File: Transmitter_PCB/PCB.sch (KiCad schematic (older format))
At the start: 47 parts, among them J1 Conn_01x04_Female, J10 Conn_01x08_Female, J11 Conn_01x01_Female, J12 Conn_01x04_Female, J13 Conn_01x02_Female, J2 Conn_01x28_Female, J3 Conn_01x02_Female, J4 Conn_01x02_Female, J5 Conn_01x02_Female, J6 Conn_01x02_Female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

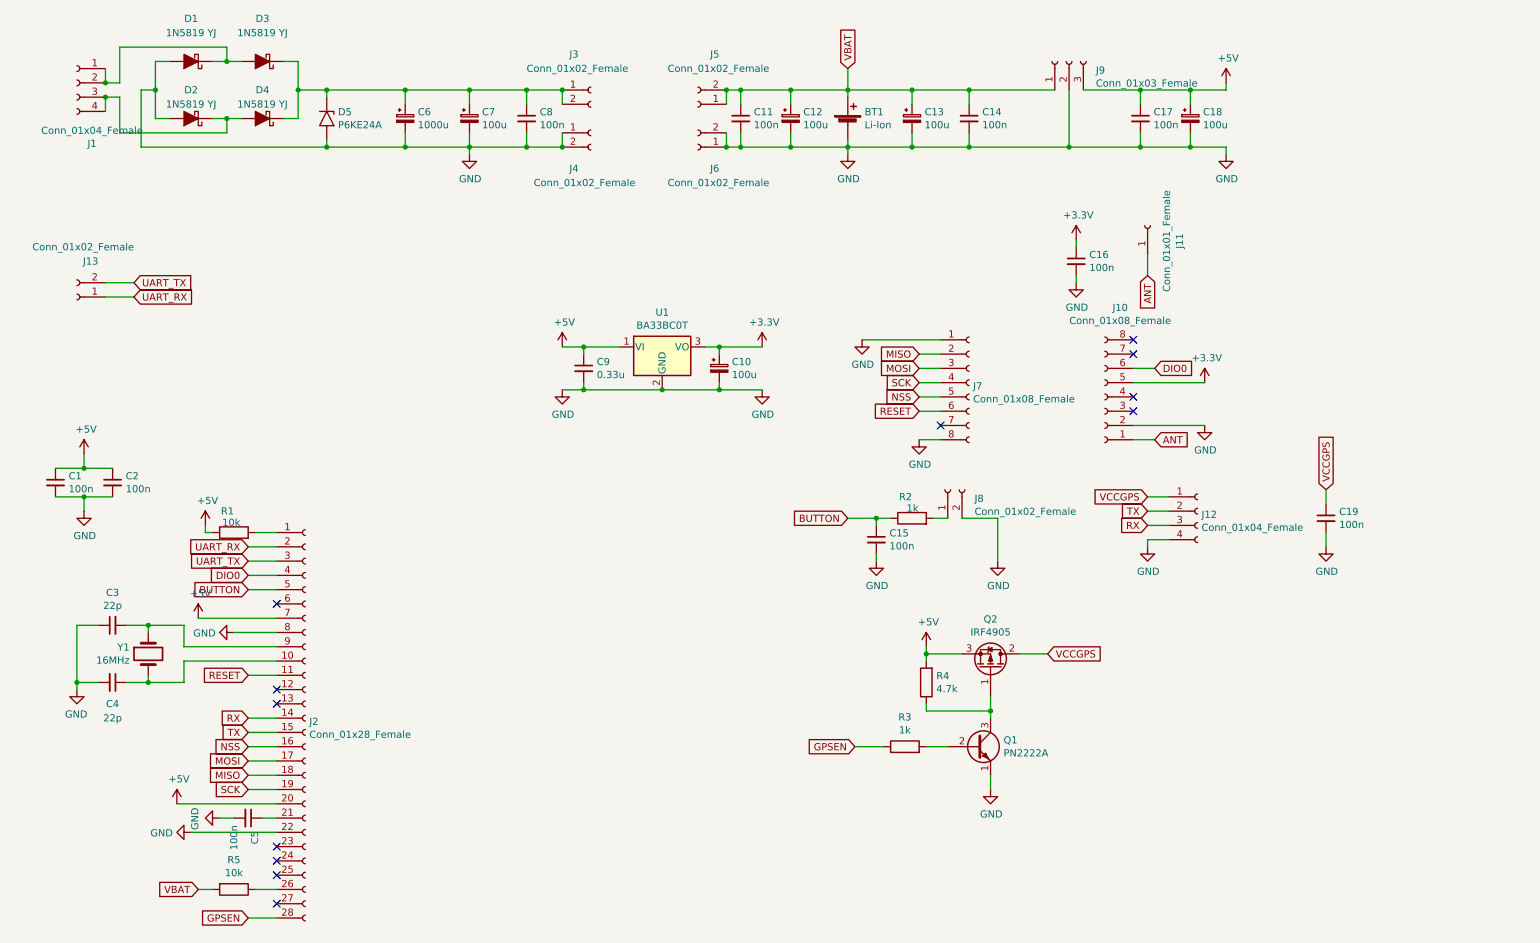
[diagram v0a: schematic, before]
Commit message: Fixed LoRa socket
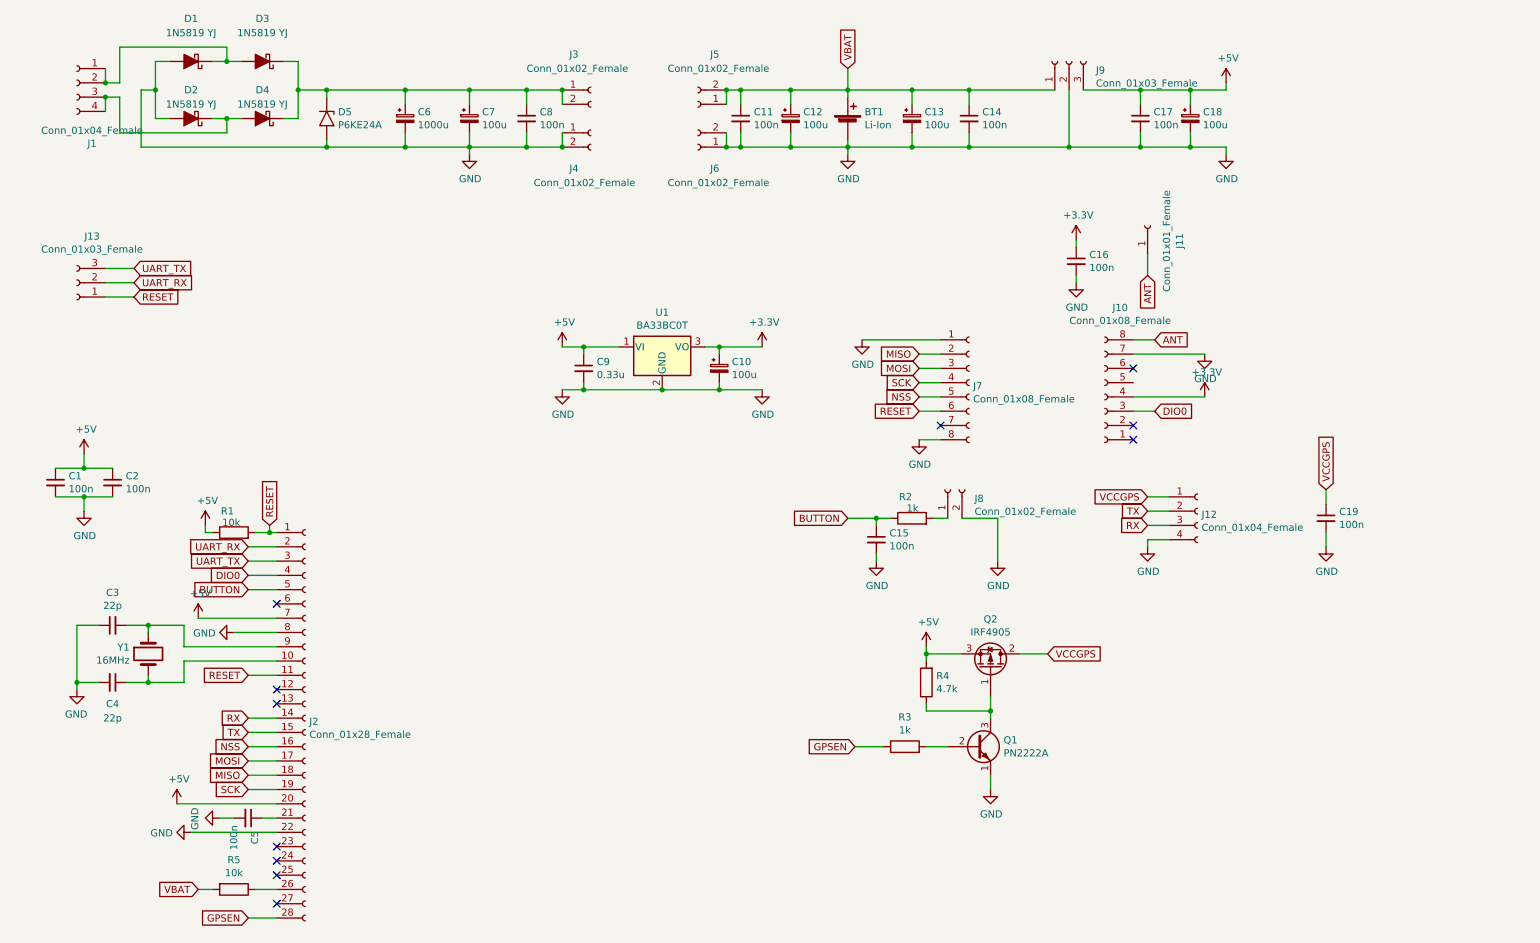
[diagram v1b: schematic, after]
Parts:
- removed J13: Conn_01x02_Female, Connector_PinSocket_2.54mm:PinSocket_1x02_P2.54mm_Vertical, symbol Connector:Conn_01x02_Female
- added J13: Conn_01x03_Female, Connector_PinSocket_2.54mm:PinSocket_1x03_P2.54mm_Vertical, symbol Connector:Conn_01x03_Female
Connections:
- net +3V3: now also J10.4 (Pin_4); no longer J10.5 (Pin_5)
- net ANT: now also J10.8 (Pin_8); no longer J10.1 (Pin_1)
- net DIO0: now also J10.3 (Pin_3); no longer J10.6 (Pin_6)
- net GND: now also J10.7 (Pin_7); no longer J10.2 (Pin_2)
- net RESET: now also J2.1 (Pin_1), R1.2, J13.1 (Pin_1)
- net UART_RX: now also J13.2 (Pin_2)
- net UART_TX: now also J13.3 (Pin_3)
- no-connect marks 12 -> 11
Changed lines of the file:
@@
 	1    0    0    -1
 $EndComp
-NoConn ~ 8850 3000
-NoConn ~ 8850 3500
-NoConn ~ 8850 3400
-Wire Wire Line
-	9000 3200 8850 3200
-Wire Wire Line
-	9000 3700 8850 3700
-Text GLabel 9000 3200 2    50   Input ~ 0
-DIO0
-Wire Wire Line
-	8850 3300 9350 3300
+Wire Wire Line
+	9000 3000 8850 3000
+Wire Wire Line
+	8850 3400 9350 3400
 $Comp
 L power:+3.3V #PWR022
 U 1 1 5E58D10D
-P 9350 3300
-F 0 "#PWR022" H 9350 3150 50  0001 C CNN
-F 1 "+3.3V" H 9365 3473 50  0000 C CNN
-F 2 "" H 9350 3300 50  0001 C CNN
-F 3 "" H 9350 3300 50  0001 C CNN
-	1    9350 3300
-	1    0    0    -1
-$EndComp
-Wire Wire Line
-	8850 3600 9350 3600
-$Comp
-L power:GND #PWR023
-U 1 1 5E5A485A
-P 9350 3600
-F 0 "#PWR023" H 9350 3350 50  0001 C CNN
-F 1 "GND" H 9355 3427 50  0000 C CNN
-F 2 "" H 9350 3600 50  0001 C CNN
-F 3 "" H 9350 3600 50  0001 C CNN
-	1    9350 3600
+P 9350 3400
+F 0 "#PWR022" H 9350 3250 50  0001 C CNN
+F 1 "+3.3V" H 9365 3573 50  0000 C CNN
+F 2 "" H 9350 3400 50  0001 C CNN
+F 3 "" H 9350 3400 50  0001 C CNN
+	1    9350 3400
 	1    0    0    -1
 $EndComp
@@
 	0    -1   -1   0
 $EndComp
-Text GLabel 9000 3700 2    50   Input ~ 0
+Text GLabel 9000 3000 2    50   Input ~ 0
 ANT
 Wire Wire Line
@@
 ANT
 Wire Wire Line
-	2700 4350 2850 4350
+	2700 4350 2800 4350
 $Comp
 L Device:R R1
@@
 Connection ~ 1650 1200
 Connection ~ 1650 1300
-NoConn ~ 8850 3100
-$Comp
-L Connector:Conn_01x02_Female J13
-U 1 1 5E38F499
-P 1450 2700
-F 0 "J13" H 1300 2450 50  0000 L CNN
-F 1 "Conn_01x02_Female" H 1050 2350 50  0000 L CNN
-F 2 "Connector_PinSocket_2.54mm:PinSocket_1x02_P2.54mm_Vertical" H 1450 2700 50  0001 C CNN
-F 3 "~" H 1450 2700 50  0001 C CNN
-	1    1450 2700
-	-1   0    0    1
-$EndComp
 Text GLabel 2650 4450 0    50   Input ~ 0
 UART_RX
@@
 Wire Wire Line
 	2850 4550 2650 4550
-Text GLabel 1850 2700 2    50   Input ~ 0
+Text GLabel 1850 2600 2    50   Input ~ 0
 UART_RX
-Wire Wire Line
-	1650 2700 1850 2700
-Text GLabel 1850 2600 2    50   Input ~ 0
+Text GLabel 1850 2500 2    50   Input ~ 0
 UART_TX
-Wire Wire Line
-	1650 2600 1850 2600
 $Comp
 L Device:R R5
@@
 Text GLabel 2300 6850 0    50   Input ~ 0
 VBAT
+NoConn ~ 8850 3700
+NoConn ~ 8850 3600
+Wire Wire Line
+	9000 3500 8850 3500
+Text GLabel 9000 3500 2    50   Input ~ 0
+DIO0
+NoConn ~ 8850 3200
+Wire Wire Line
+	8850 3100 9350 3100
+$Comp
+L power:GND #PWR0101
+U 1 1 5E431489
+P 9350 3100
+F 0 "#PWR0101" H 9350 2850 50  0001 C CNN
+F 1 "GND" H 9355 2927 50  0000 C CNN
+F 2 "" H 9350 3100 50  0001 C CNN
+F 3 "" H 9350 3100 50  0001 C CNN
+	1    9350 3100
+	1    0    0    -1
+$EndComp
+$Comp
+L Connector:Conn_01x03_Female J13
+U 1 1 5E44D686
+P 1450 2600
+F 0 "J13" H 1344 2275 50  0000 C CNN
+F 1 "Conn_01x03_Female" H 1344 2366 50  0000 C CNN
+F 2 "Connector_PinSocket_2.54mm:PinSocket_1x03_P2.54mm_Vertical" H 1450 2600 50  0001 C CNN
+F 3 "~" H 1450 2600 50  0001 C CNN
+	1    1450 2600
+	-1   0    0    1
+$EndComp
+Text GLabel 2800 4300 1    50   Input ~ 0
+RESET
+Wire Wire Line
+	2800 4350 2800 4300
+Connection ~ 2800 4350
+Wire Wire Line
+	2800 4350 2850 4350
+Wire Wire Line
+	1650 2700 1850 2700
+Text GLabel 1850 2700 2    50   Input ~ 0
+RESET
+Wire Wire Line
+	1650 2500 1850 2500
+Wire Wire Line
+	1650 2600 1850 2600
 $EndSCHEMATC

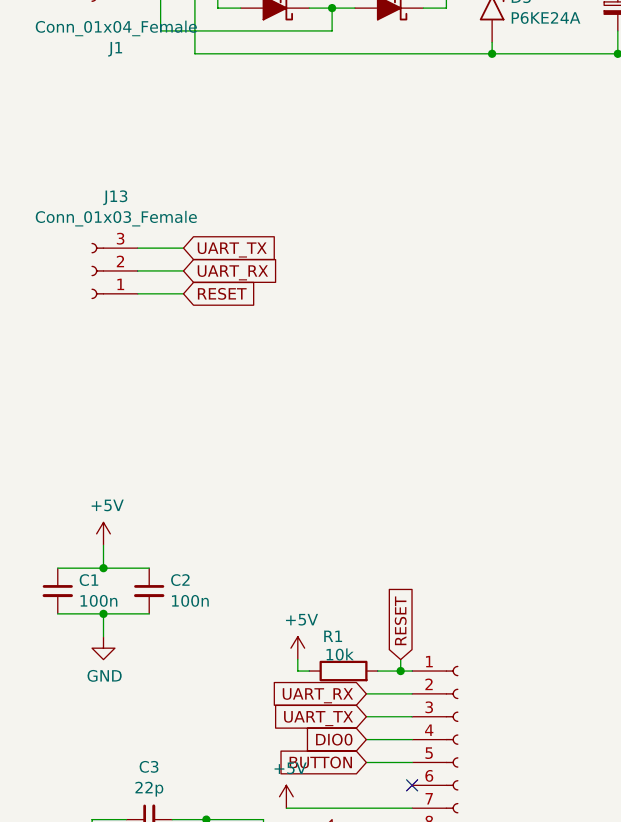
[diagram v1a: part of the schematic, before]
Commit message: Fixed Transmitter PCB Spacing
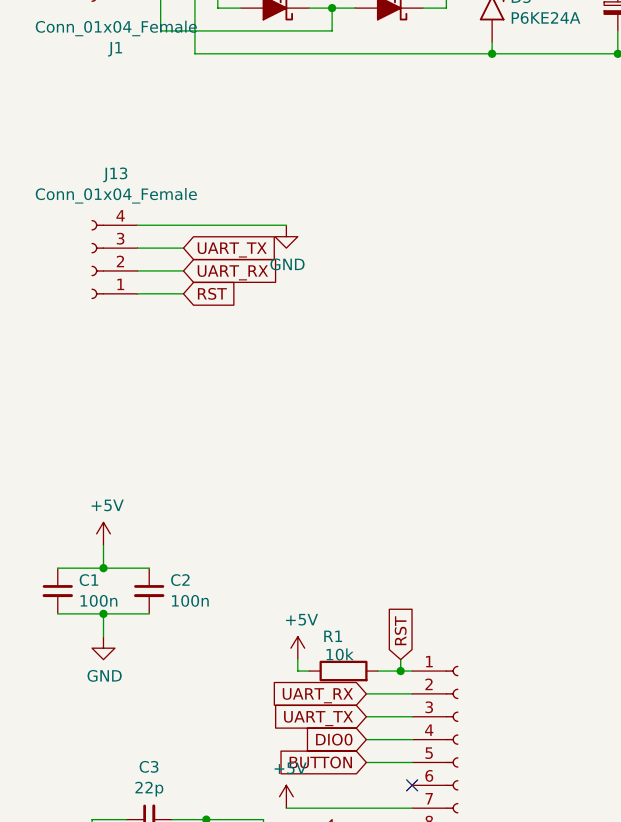
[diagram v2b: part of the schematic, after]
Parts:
- removed J13: Conn_01x03_Female, Connector_PinSocket_2.54mm:PinSocket_1x03_P2.54mm_Vertical, symbol Connector:Conn_01x03_Female
- added J13: Conn_01x04_Female, Connector_PinSocket_2.54mm:PinSocket_1x04_P2.54mm_Vertical, symbol Connector:Conn_01x04_Female
- J8: footprint Connector_Molex:Molex_PicoBlade_53047-0210_1x02_P1.25mm_Vertical -> Connector_Molex:Molex_KK-254_AE-6410-02A_1x02_P2.54mm_Vertical
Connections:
- net GND: now also J13.4 (Pin_4)
- net RESET: no longer J2.1 (Pin_1), R1.2
- net UART_RX: now also J13.2 (Pin_2)
- net UART_TX: now also J13.3 (Pin_3)
- new net RST: J13.1 (Pin_1), J2.1 (Pin_1), R1.2
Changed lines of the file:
@@
 F 0 "J8" V 7488 3862 50  0000 R CNN
 F 1 "Conn_01x02_Female" V 7397 3862 50  0000 R CNN
-F 2 "Connector_Molex:Molex_PicoBlade_53047-0210_1x02_P1.25mm_Vertical" H 7550 4050 50  0001 C CNN
+F 2 "Connector_Molex:Molex_KK-254_AE-6410-02A_1x02_P2.54mm_Vertical" H 7550 4050 50  0001 C CNN
 F 3 "~" H 7550 4050 50  0001 C CNN
 	1    7550 4050
@@
 Connection ~ 6000 1250
 Connection ~ 6000 1650
-Wire Wire Line
-	7700 1650 8400 1650
 Connection ~ 8400 1650
 Wire Wire Line
@@
 	8400 1250 8400 1650
 Wire Wire Line
-	7700 1250 8300 1250
-Wire Wire Line
 	8500 1250 8900 1250
 NoConn ~ 2850 6650
@@
 	1    0    0    -1
 $EndComp
-$Comp
-L Connector:Conn_01x03_Female J13
-U 1 1 5E44D686
+Text GLabel 2800 4300 1    50   Input ~ 0
+RST
+Wire Wire Line
+	2800 4350 2800 4300
+Connection ~ 2800 4350
+Wire Wire Line
+	2800 4350 2850 4350
+Wire Wire Line
+	1650 2700 1850 2700
+Text GLabel 1850 2700 2    50   Input ~ 0
+RST
+Wire Wire Line
+	1650 2500 1850 2500
+Wire Wire Line
+	1650 2600 1850 2600
+Wire Wire Line
+	7700 1650 8400 1650
+Wire Wire Line
+	7700 1250 8300 1250
+$Comp
+L Connector:Conn_01x04_Female J13
+U 1 1 5E4E3087
 P 1450 2600
-F 0 "J13" H 1344 2275 50  0000 C CNN
-F 1 "Conn_01x03_Female" H 1344 2366 50  0000 C CNN
-F 2 "Connector_PinSocket_2.54mm:PinSocket_1x03_P2.54mm_Vertical" H 1450 2600 50  0001 C CNN
+F 0 "J13" H 1344 2175 50  0000 C CNN
+F 1 "Conn_01x04_Female" H 1344 2266 50  0000 C CNN
+F 2 "Connector_PinSocket_2.54mm:PinSocket_1x04_P2.54mm_Vertical" H 1450 2600 50  0001 C CNN
 F 3 "~" H 1450 2600 50  0001 C CNN
 	1    1450 2600
 	-1   0    0    1
 $EndComp
-Text GLabel 2800 4300 1    50   Input ~ 0
-RESET
-Wire Wire Line
-	2800 4350 2800 4300
-Connection ~ 2800 4350
-Wire Wire Line
-	2800 4350 2850 4350
-Wire Wire Line
-	1650 2700 1850 2700
-Text GLabel 1850 2700 2    50   Input ~ 0
-RESET
-Wire Wire Line
-	1650 2500 1850 2500
-Wire Wire Line
-	1650 2600 1850 2600
+Wire Wire Line
+	1650 2400 2300 2400
+$Comp
+L power:GND #PWR0102
+U 1 1 5E4FFF60
+P 2300 2400
+F 0 "#PWR0102" H 2300 2150 50  0001 C CNN
+F 1 "GND" H 2305 2227 50  0000 C CNN
+F 2 "" H 2300 2400 50  0001 C CNN
+F 3 "" H 2300 2400 50  0001 C CNN
+	1    2300 2400
+	1    0    0    -1
+$EndComp
 $EndSCHEMATC

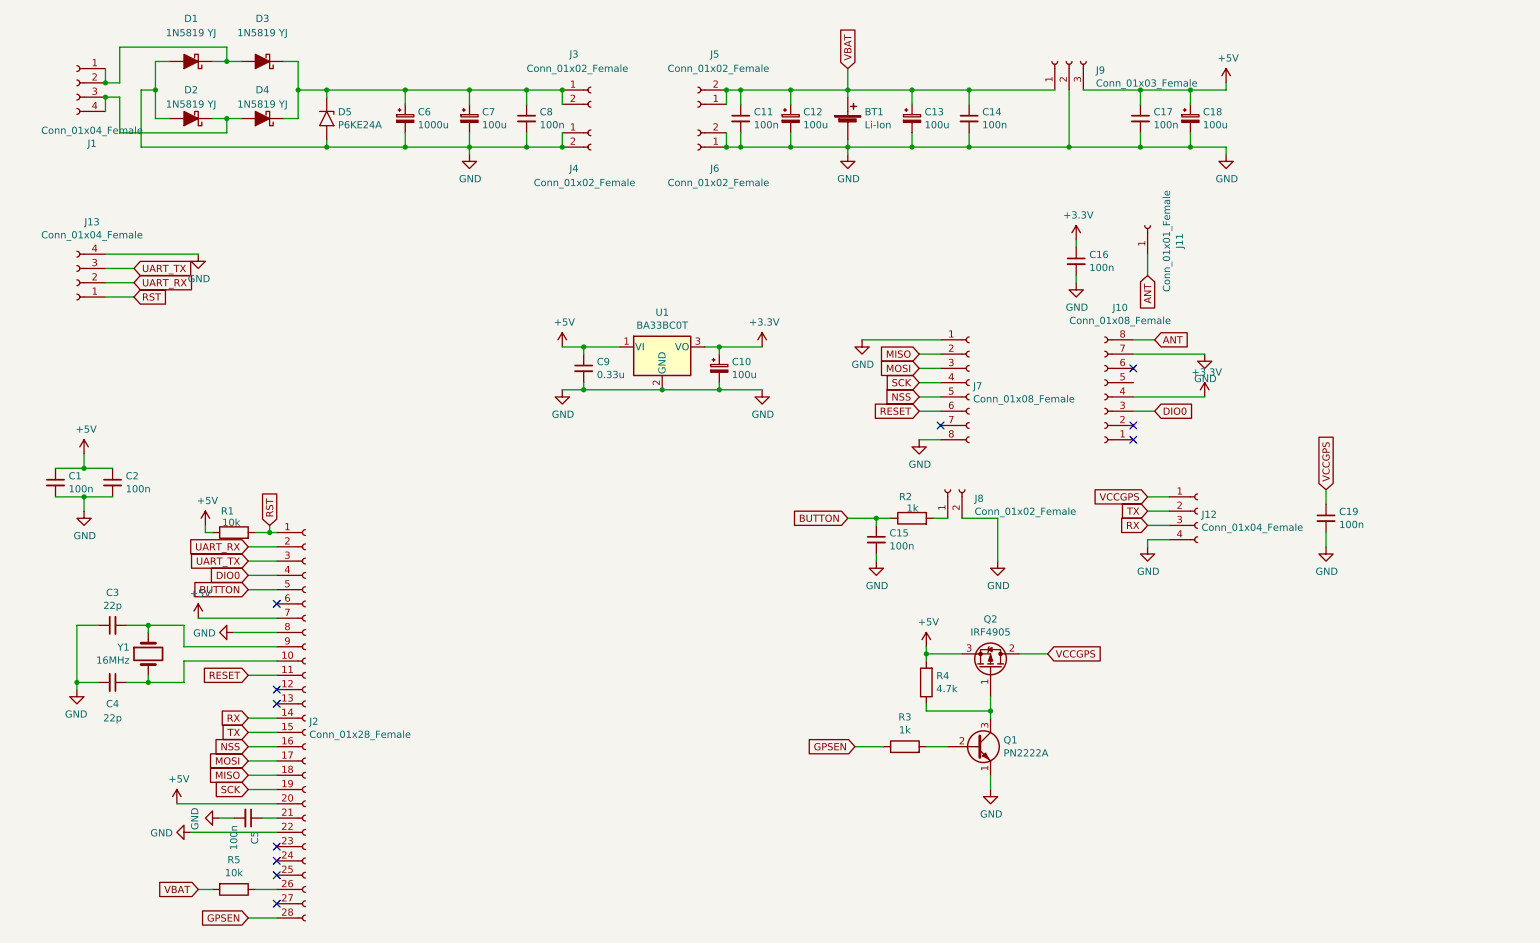
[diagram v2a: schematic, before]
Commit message: Added 3d models
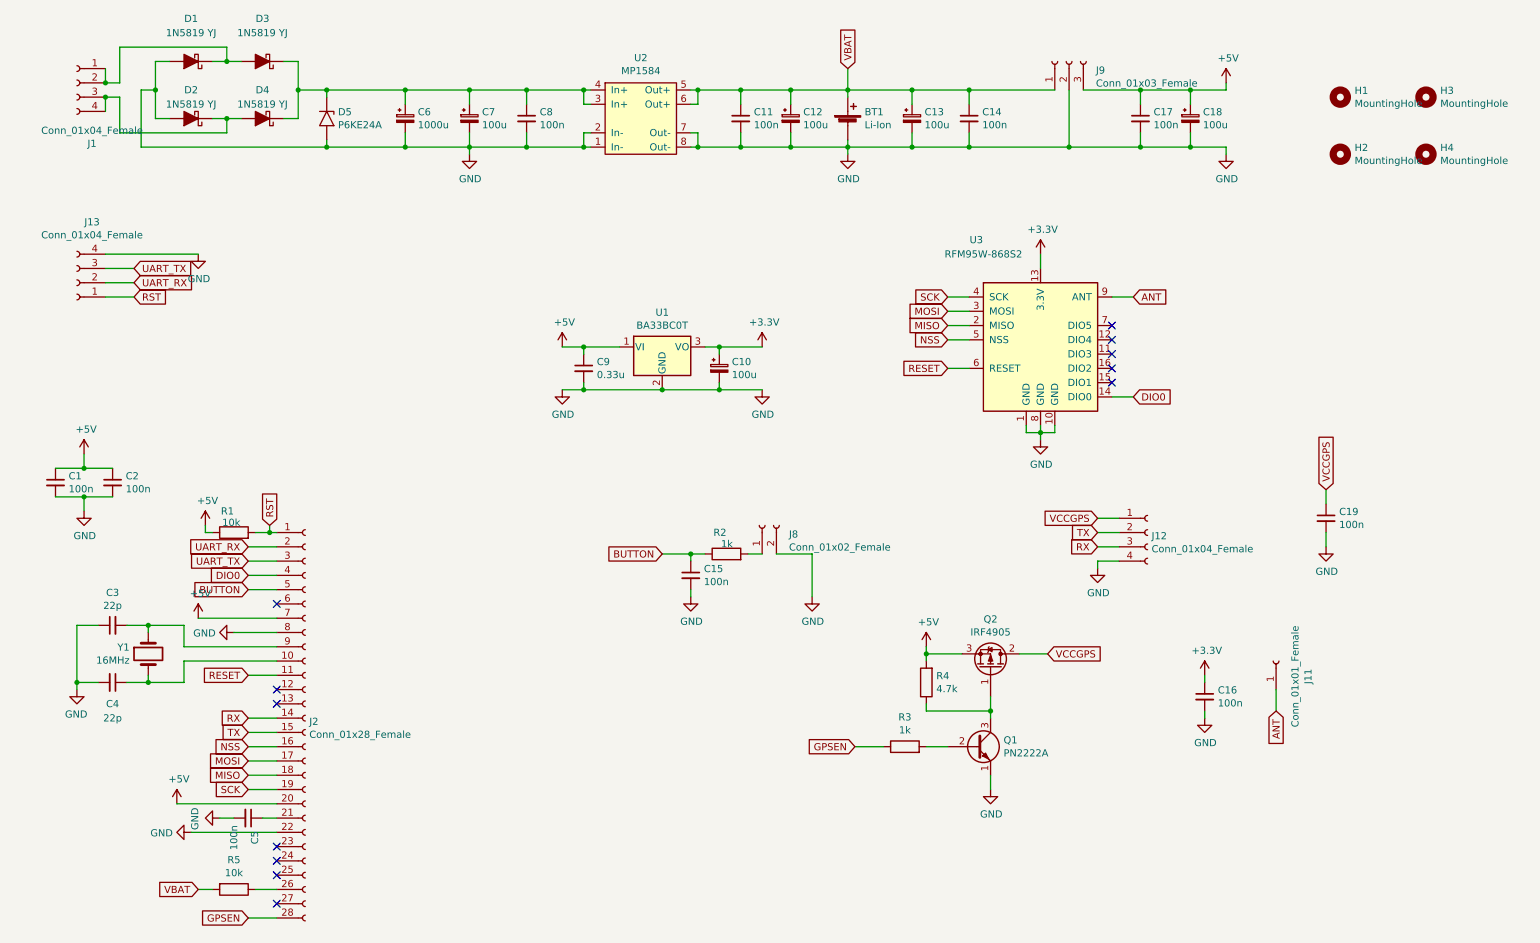
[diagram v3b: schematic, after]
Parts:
- removed J10, J7: Conn_01x08_Female, Connector_PinSocket_2.00mm:PinSocket_1x08_P2.00mm_Vertical, symbol Connector:Conn_01x08_Female
- removed J3, J4, J5, J6: Conn_01x02_Female, Connector_PinSocket_2.54mm:PinSocket_1x02_P2.54mm_Vertical, symbol Connector:Conn_01x02_Female
- added H1, H2, H3, H4: MountingHole, MountingHole:MountingHole_3.5mm_Pad_Via, symbol Mechanical:MountingHole
- added U2: MP1584, MyComponents:MP1584, symbol MyComponents:MP1584
- added U3: RFM95W-868S2, MyComponents:RFM95W_THT, symbol RF_Module:RFM95W-868S2
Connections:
- net +3V3: now also U3.13 (3.3V)
- net ANT: now also U3.9 (ANT)
- net DIO0: now also U3.14 (DIO0)
- net GND: now also U2.1 (In-), U2.2 (In-), U2.7 (Out-), U2.8 (Out-), U3.1 (GND), U3.10 (GND), U3.8 (GND)
- net MISO: now also U3.2 (MISO)
- net MOSI: now also U3.3 (MOSI)
- net NSS: now also U3.5 (NSS)
- net RESET: now also U3.6 (RESET)
- net SCK: now also U3.4 (SCK)
- net VBAT: now also U2.5 (Out+), U2.6 (Out+)
- net at C6.1, C7.1, C8.1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: now also U2.3 (In+), U2.4 (In+)
- no-connect marks 11 -> 12
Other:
- moved on the sheet: C15, C16, J11, J12, J8, R2

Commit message: Added changes to schematics
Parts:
- added J3: Conn_01x03_Female, symbol Connector:Conn_01x03_Female
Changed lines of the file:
@@
 EESchema Schematic File Version 4
 LIBS:PCB-cache
-EELAYER 29 0
+EELAYER 26 0
 EELAYER END
 $Descr A4 11693 8268
@@
 NoConn ~ 8700 3000
 NoConn ~ 8700 2900
+$Comp
+L Connector:Conn_01x03_Female J3
+U 1 1 5E40F892
+P 10200 2250
+F 0 "J3" H 10227 2276 50  0000 L CNN
+F 1 "Conn_01x03_Female" H 10227 2185 50  0000 L CNN
+F 2 "" H 10200 2250 50  0001 C CNN
+F 3 "~" H 10200 2250 50  0001 C CNN
+	1    10200 2250
+	1    0    0    -1
+$EndComp
 $EndSCHEMATC
